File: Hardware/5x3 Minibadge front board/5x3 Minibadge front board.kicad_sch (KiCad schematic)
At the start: 1 part, among them J1 Board to Board

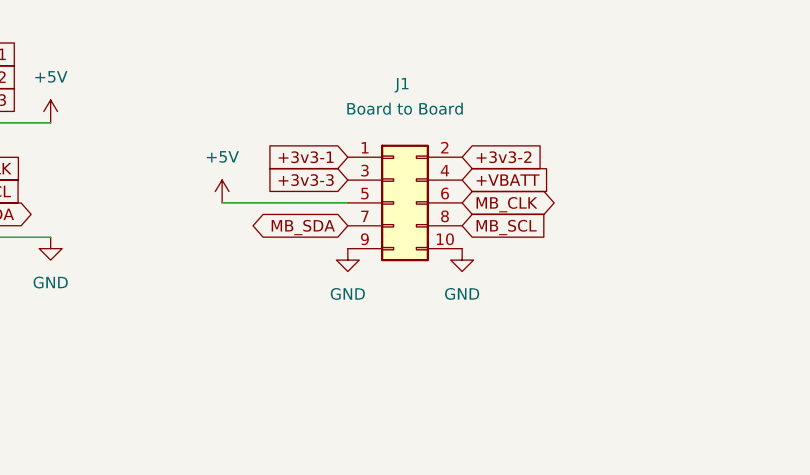
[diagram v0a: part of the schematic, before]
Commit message: Routed Minibadge Display
god that sucked, and my routing sucks too.
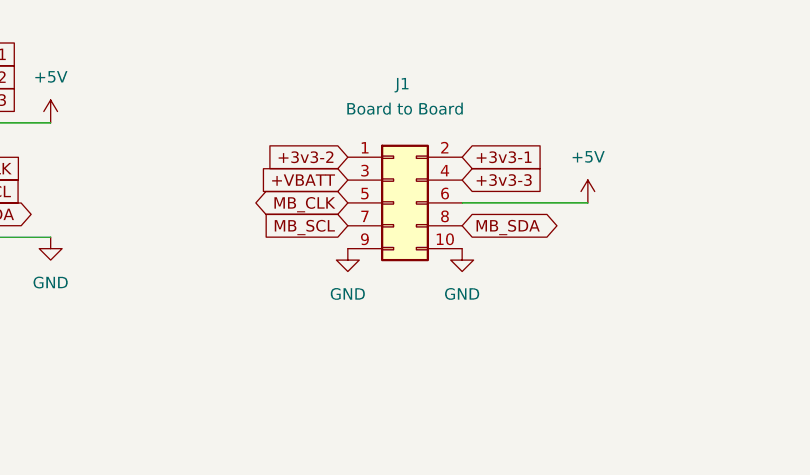
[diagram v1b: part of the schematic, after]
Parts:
- J1: footprint (none) -> Connector_PinHeader_2.54mm:PinHeader_2x05_P2.54mm_Vertical_SMD
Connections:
- net +3v3-1: now also J1.2 (Pin_2); no longer J1.1 (Pin_1)
- net +3v3-2: now also J1.1 (Pin_1); no longer J1.2 (Pin_2)
- net +3v3-3: now also J1.4 (Pin_4); no longer J1.3 (Pin_3)
- net +5V: now also J1.6 (Pin_6); no longer J1.5 (Pin_5)
- net +VBATT: now also J1.3 (Pin_3); no longer J1.4 (Pin_4)
- net MB_CLK: now also J1.5 (Pin_5); no longer J1.6 (Pin_6)
- net MB_SCL: now also J1.7 (Pin_7); no longer J1.8 (Pin_8)
- net MB_SDA: now also J1.8 (Pin_8); no longer J1.7 (Pin_7)
